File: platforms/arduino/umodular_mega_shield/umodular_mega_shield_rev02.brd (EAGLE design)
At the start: 53.5 x 100 mm, 31 parts, among them IC1 23LC1024, IC2 74HC4050/CD4050, IC3 6N138, U1 ARDUINO-MEGA-SHIELD

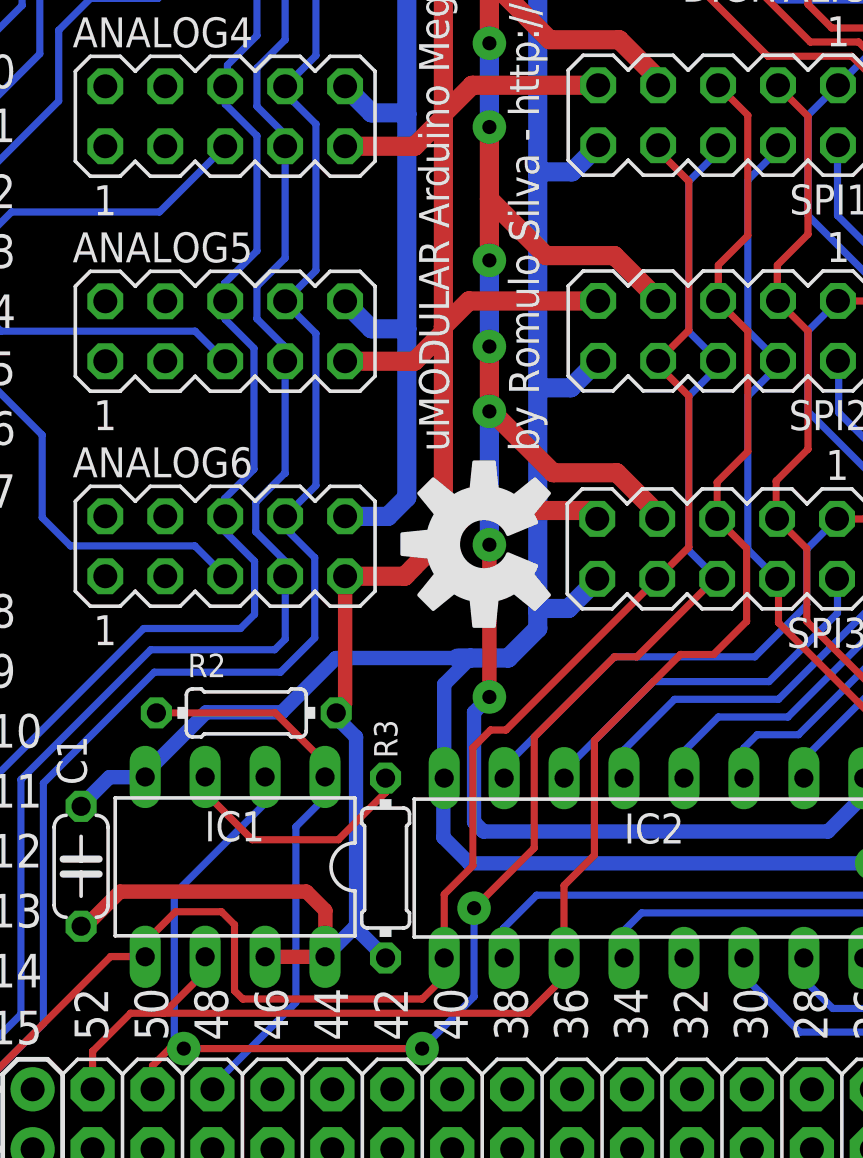
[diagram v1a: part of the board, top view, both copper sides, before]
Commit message: changes that reflects main hardware connections of project. Hardware SPI are only for RAM memory, sdcard goes via SoftSPI(exclusive wire path) and shift registers 165 and 595 goes via shiftIn and shiftOut
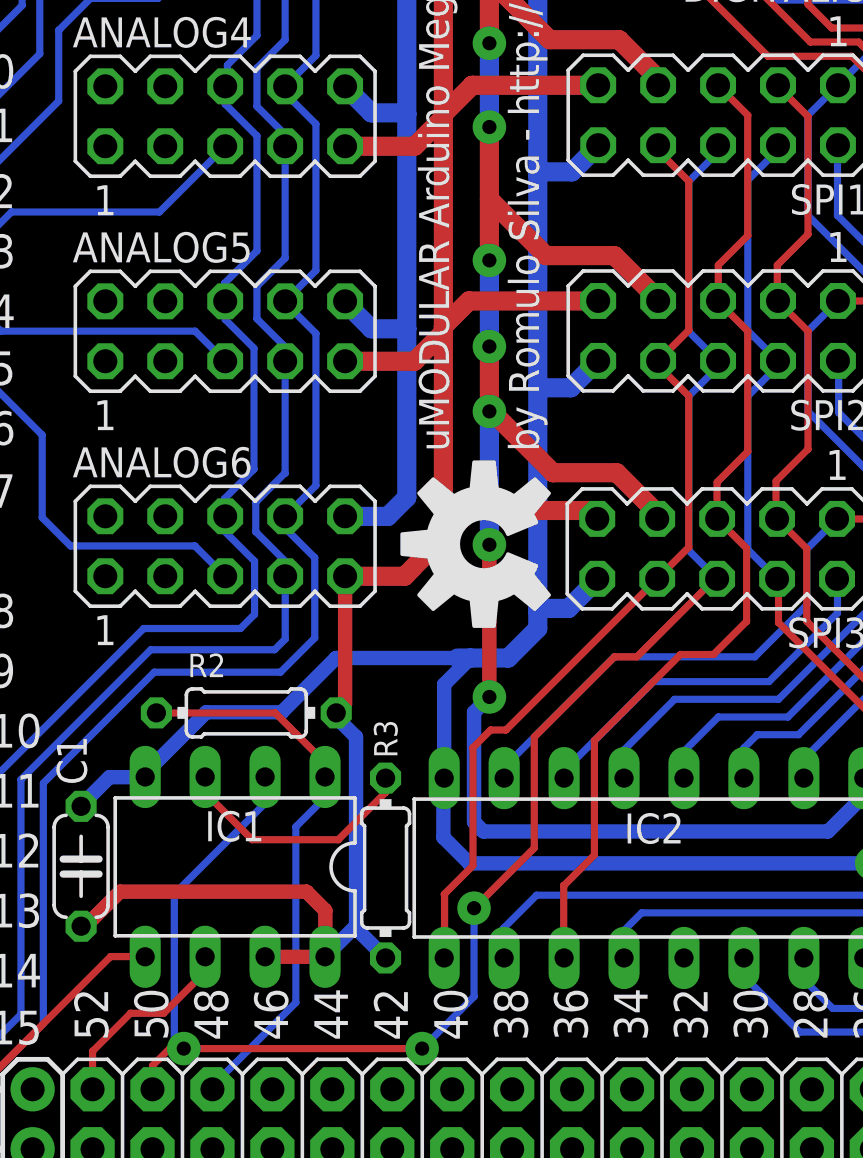
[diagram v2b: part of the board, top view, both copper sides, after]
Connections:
- new net SDCARD_CLOCK: IC2.11, U1.39
- new net SDCARD_MISO: SPI1.6, U1.40
- new net SDCARD_MOSI: IC2.9, U1.38
- net SPI_CLOCK: no longer IC2.11
- net SPI_MISO: no longer SPI1.6
- net SPI_MOSI: no longer IC2.9
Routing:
- net SPI_CLOCK: track 70.5 -> 52.9 mm
- net SPI_MOSI: track 80.6 -> 63.2 mm
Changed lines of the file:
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@@
 <wire x1="10.285" y1="8.225" x2="10.285" y2="9.835" width="0.3048" layer="1"/>
 <wire x1="10.285" y1="9.835" x2="11.9" y2="11.45" width="0.3048" layer="1"/>
-<contactref element="IC2" pad="11"/>
-<wire x1="13.3" y1="11.45" x2="28.75" y2="11.45" width="0.3048" layer="1"/>
+<wire x1="13.3" y1="11.45" x2="28.75" y2="11.45" width="0" layer="19" extent="1-16"/>
 <wire x1="11.9" y1="11.45" x2="13.3" y2="11.45" width="0.3048" layer="1"/>
 <wire x1="13.3" y1="11.45" x2="15" y2="13.15" width="0.3048" layer="1"/>
 <wire x1="15" y1="13.15" x2="15" y2="13.785" width="0.3048" layer="1"/>
 <wire x1="15" y1="13.785" x2="15.055" y2="13.84" width="0.3048" layer="1"/>
-<wire x1="28.75" y1="11.45" x2="30.25" y2="12.95" width="0.3048" layer="1"/>
-<wire x1="30.25" y1="12.95" x2="30.25" y2="13.775" width="0.3048" layer="1"/>
-<wire x1="30.25" y1="13.775" x2="30.265" y2="13.79" width="0.3048" layer="1"/>
+<wire x1="28.75" y1="11.45" x2="30.25" y2="12.95" width="0" layer="19" extent="1-16"/>
 <wire x1="36.79" y1="50.77" x2="36.79" y2="50.76" width="0.3048" layer="1"/>
 <wire x1="36.79" y1="50.76" x2="38.05" y2="49.5" width="0.3048" layer="1"/>
@@
 <wire x1="38.05" y1="35.25" x2="36.75" y2="33.95" width="0.3048" layer="1"/>
 <wire x1="36.75" y1="33.95" x2="36.75" y2="32.395" width="0.3048" layer="1"/>
-<wire x1="30.265" y1="13.79" x2="30.265" y2="16.865" width="0.3048" layer="1"/>
 <wire x1="30.265" y1="16.865" x2="31.55" y2="18.15" width="0.3048" layer="1"/>
 <wire x1="31.55" y1="18.15" x2="31.55" y2="23" width="0.3048" layer="1"/>
@@
 <wire x1="38" y1="28.05" x2="38" y2="31.145" width="0.3048" layer="1"/>
 <wire x1="38" y1="31.145" x2="36.75" y2="32.395" width="0.3048" layer="1"/>
+<wire x1="30.265" y1="16.865" x2="30.25" y2="16.865" width="0.3048" layer="1"/>
+<wire x1="30.25" y1="16.865" x2="30.25" y2="12.95" width="0.3048" layer="1"/>
 </signal>
 <signal name="SPI_MISO">
-<contactref element="SPI1" pad="6"/>
 <contactref element="U1" pad="50"/>
 <contactref element="IC1" pad="2"/>
@@
 <wire x1="13.55" y1="9.95" x2="14.15" y2="9.95" width="0.3048" layer="1"/>
 <wire x1="13.75" y1="10.35" x2="14.15" y2="9.95" width="0.3048" layer="16"/>
-<wire x1="36.79" y1="48.23" x2="36.79" y2="47.94" width="0.3048" layer="16"/>
 <wire x1="36.79" y1="47.94" x2="35.55" y2="46.7" width="0.3048" layer="16"/>
 <wire x1="35.55" y1="46.7" x2="35.55" y2="40.33" width="0.3048" layer="16"/>
@@
 <wire x1="5.35" y1="5.5" x2="5.35" y2="8.15" width="0.3048" layer="1"/>
 <wire x1="5.35" y1="8.15" x2="11.05" y2="13.85" width="0.3048" layer="1"/>
-<contactref element="IC2" pad="9"/>
 <wire x1="11.05" y1="13.85" x2="12.505" y2="13.85" width="0.3048" layer="1"/>
 <wire x1="12.505" y1="13.85" x2="12.515" y2="13.84" width="0.3048" layer="1"/>
-<wire x1="12.515" y1="13.84" x2="12.515" y2="14.465" width="0.3048" layer="1"/>
-<wire x1="12.515" y1="14.465" x2="13.8" y2="15.75" width="0.3048" layer="1"/>
-<wire x1="13.8" y1="15.75" x2="15.75" y2="15.75" width="0.3048" layer="1"/>
-<wire x1="15.75" y1="15.75" x2="16.3" y2="15.2" width="0.3048" layer="1"/>
-<wire x1="16.3" y1="15.2" x2="16.3" y2="12.4" width="0.3048" layer="1"/>
-<wire x1="16.3" y1="12.4" x2="16.65" y2="12.05" width="0.3048" layer="1"/>
-<wire x1="16.65" y1="12.05" x2="24.25" y2="12.05" width="0.3048" layer="1"/>
-<wire x1="24.25" y1="12.05" x2="25.2" y2="13" width="0.3048" layer="1"/>
-<wire x1="25.2" y1="13" x2="25.2" y2="13.775" width="0.3048" layer="1"/>
-<wire x1="25.2" y1="13.775" x2="25.185" y2="13.79" width="0.3048" layer="1"/>
+<wire x1="12.515" y1="13.84" x2="12.515" y2="14.465" width="0" layer="19" extent="1-16"/>
+<wire x1="12.515" y1="14.465" x2="13.8" y2="15.75" width="0" layer="19" extent="1-16"/>
+<wire x1="13.8" y1="15.75" x2="15.75" y2="15.75" width="0" layer="19" extent="1-16"/>
+<wire x1="15.75" y1="15.75" x2="16.3" y2="15.2" width="0" layer="19" extent="1-16"/>
+<wire x1="16.3" y1="15.2" x2="16.3" y2="12.4" width="0" layer="19" extent="1-16"/>
+<wire x1="16.3" y1="12.4" x2="16.65" y2="12.05" width="0" layer="19" extent="1-16"/>
+<wire x1="16.65" y1="12.05" x2="24.25" y2="12.05" width="0" layer="19" extent="1-16"/>
+<wire x1="24.25" y1="12.05" x2="25.2" y2="13" width="0" layer="19" extent="1-16"/>
 <wire x1="34.25" y1="48.23" x2="34.25" y2="48" width="0.3048" layer="1"/>
 <wire x1="34.25" y1="48" x2="35.55" y2="46.7" width="0.3048" layer="1"/>
@@
 <wire x1="35.55" y1="37.6" x2="35.55" y2="31.195" width="0.3048" layer="1"/>
 <wire x1="35.55" y1="31.195" x2="34.21" y2="29.855" width="0.3048" layer="1"/>
-<wire x1="25.185" y1="13.79" x2="25.185" y2="16.485" width="0.3048" layer="1"/>
 <wire x1="25.185" y1="16.485" x2="26.4" y2="17.7" width="0.3048" layer="1"/>
 <wire x1="26.4" y1="17.7" x2="26.4" y2="22.7" width="0.3048" layer="1"/>
@@
 <wire x1="27.15" y1="23.45" x2="27.805" y2="23.45" width="0.3048" layer="1"/>
 <wire x1="27.805" y1="23.45" x2="34.21" y2="29.855" width="0.3048" layer="1"/>
+<wire x1="25.185" y1="16.485" x2="25.2" y2="16.485" width="0.3048" layer="1"/>
+<wire x1="25.2" y1="16.485" x2="25.2" y2="13" width="0.3048" layer="1"/>
 </signal>
 <signal name="SPI_SS3">
@@
 <wire x1="45.495" y1="57.245" x2="41.87" y2="57.245" width="0.3048" layer="16"/>
 </signal>
+<signal name="SDCARD_MOSI">
+<contactref element="U1" pad="38"/>
+<contactref element="IC2" pad="9"/>
+<wire x1="25.185" y1="13.79" x2="28.065" y2="8.225" width="0" layer="19" extent="1-1"/>
+</signal>
+<signal name="SDCARD_CLOCK">
+<contactref element="U1" pad="39"/>
+<contactref element="IC2" pad="11"/>
+<wire x1="28.065" y1="5.685" x2="30.265" y2="13.79" width="0" layer="19" extent="1-1"/>
+</signal>
+<signal name="SDCARD_MISO">
+<contactref element="U1" pad="40"/>
+<contactref element="SPI1" pad="6"/>
+<wire x1="25.525" y1="8.225" x2="36.79" y2="48.23" width="0" layer="19" extent="1-1"/>
+</signal>
 </signals>
